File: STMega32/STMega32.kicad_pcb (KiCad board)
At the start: 2 copper layers, 49.9 x 16 mm, 15 parts, among them J1 Conn_01x20, J2 Conn_01x20, Q1 2SC4213, U1 STM32F303R6Tx, U2 LD3985M33R_SOT23

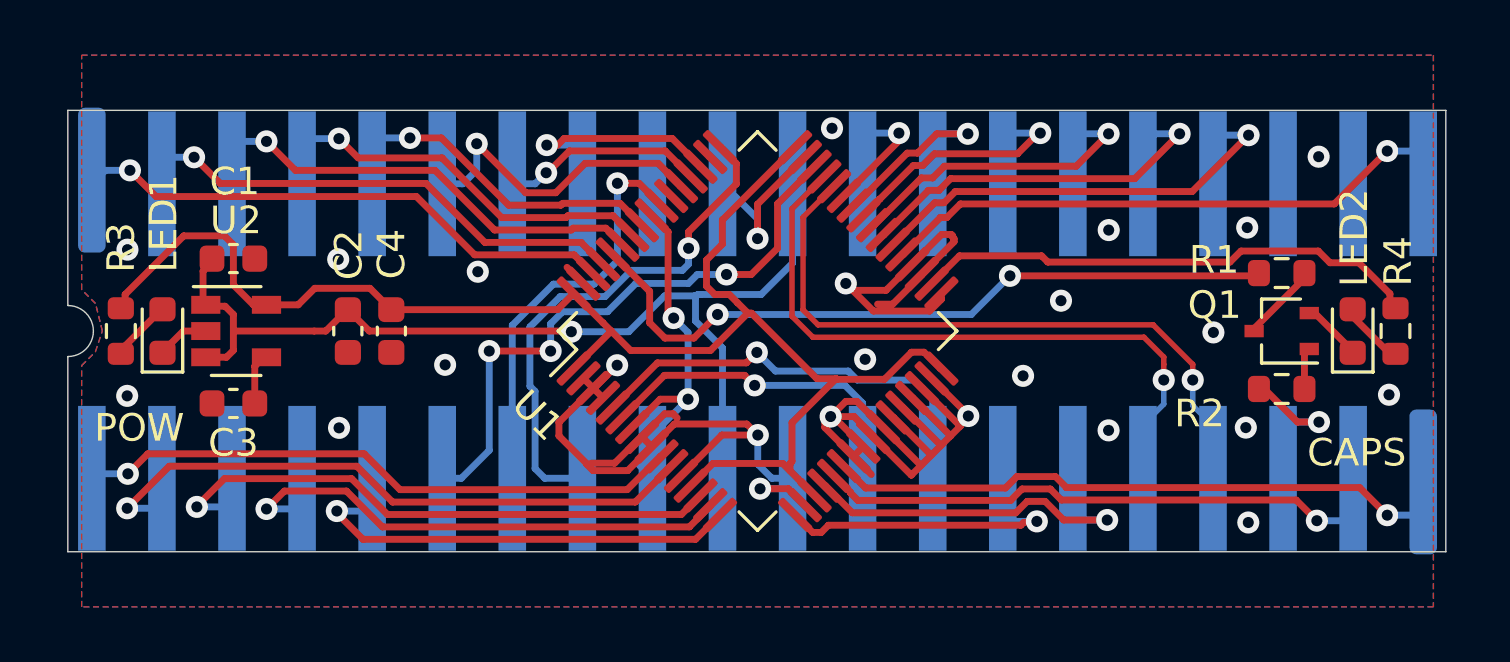
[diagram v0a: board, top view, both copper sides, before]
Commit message: Changed microcontroller and rerouted to add ground integrity
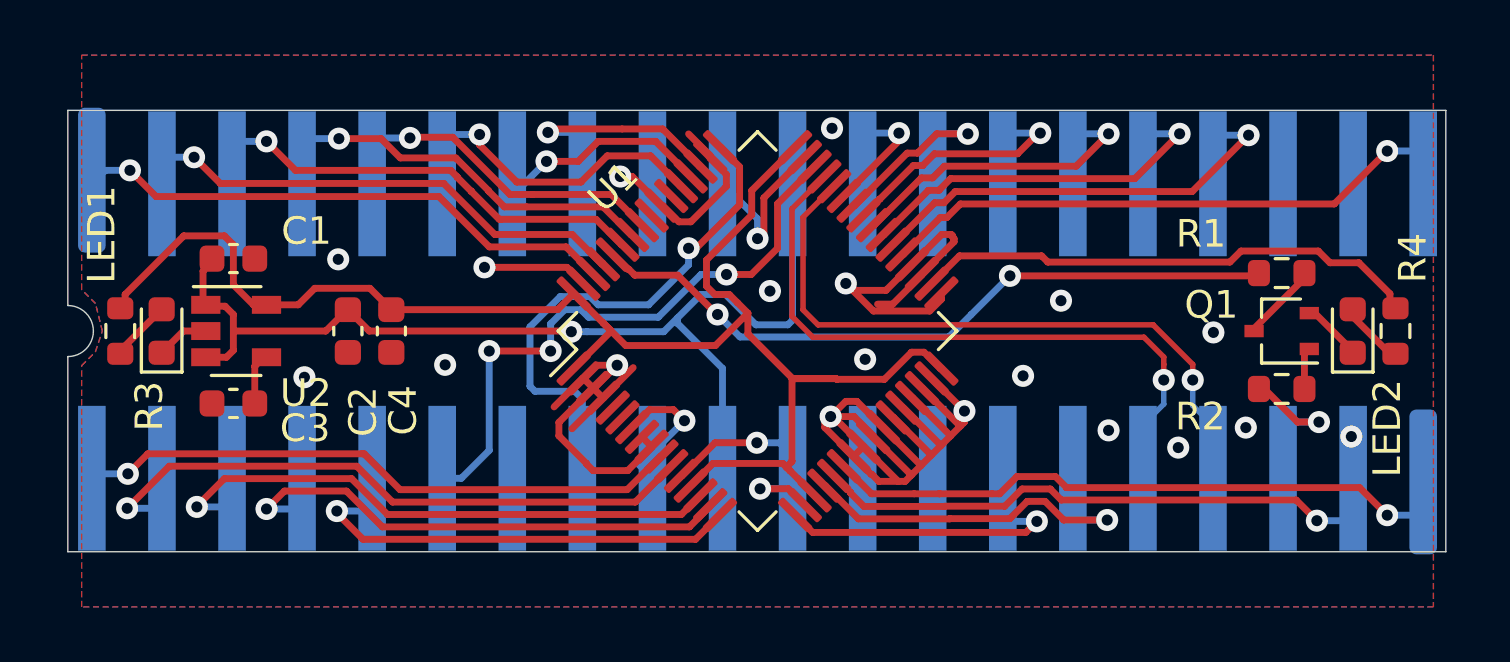
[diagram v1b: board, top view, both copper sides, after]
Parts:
- U1: value STM32F303R6Tx -> STM32F072RBTx
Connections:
- J1 pad 12: NJTRST -> Reset
- U1 pad 5: OSC_IN_2 -> Net-(U1-Pad5)
- U1 pad 50: JTDI -> GND
- U1 pad 55: MISO -> GND
- U1 pad 56: NJTRST -> Net-(U1-Pad56)
- U1 pad 6: OSC_IN_1 -> Net-(U1-Pad6)
- U1 pad 7: NJTRST -> Reset
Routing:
- net OSC_IN_2: track 16.0 -> 0.00 mm, vias 1 -> 0
- net MISO: track 15.1 -> 0.00 mm, vias 1 -> 0
- net NJTRST: track 13.8 -> 0.00 mm, vias 2 -> 0
- net OSC_IN_1: track 12.5 -> 0.00 mm, vias 1 -> 0
- net GND: track 76.9 -> 88.2 mm, vias 25 -> 21
- net Reset: track 0.00 -> 5.58 mm, vias 0 -> 1
- net +3_3v: track 56.3 -> 58.0 mm
- net +5v: track 38.0 -> 39.6 mm
- net n_boot: track 26.3 -> 25.6 mm
- net col10: track 11.4 -> 12.1 mm
- net col12: track 10.8 -> 11.4 mm
- net SCK: track 19.0 -> 19.6 mm
- net col14: track 21.3 -> 21.5 mm, vias 1 -> 2
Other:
- net class Default: clearance 0.2 -> 0.19
- rule trace_clearance: 0.2 -> 0.19
- board text removed: "5V"
- board text removed: "CAPS"
- board text removed: "CLK"
- board text removed: "GND"
- board text removed: "POW"
- board text removed: "SWDIO"
- board text removed: "SWO"
- board text removed: "USBN"
- board text removed: "USBP"

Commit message: removed unused folder, changed R2 on inverter circuit to pullup
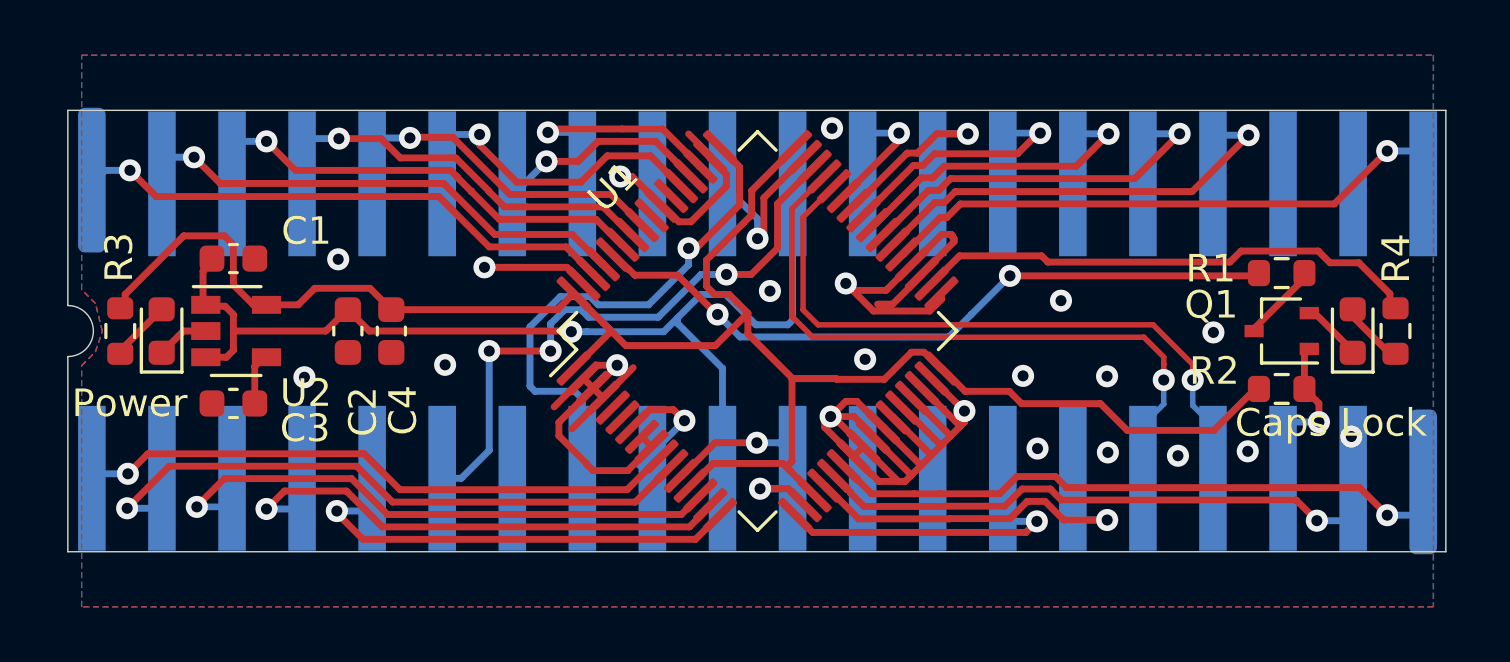
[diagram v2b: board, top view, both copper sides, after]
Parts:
- Caps Lock: renamed from LED2
- turned R2 to 180 degrees
- renumbered LED1 to Power
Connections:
- Q1 pad 1: Net-(Q1-Pad1) -> boot
- R2 pad 2: Net-(Q1-Pad1) -> +3_3v
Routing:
- net +3_3v: track 58.0 -> 71.2 mm
- net Net-(Q1-Pad1): track 1.42 -> 0.00 mm
- net GND: vias 21 -> 23
